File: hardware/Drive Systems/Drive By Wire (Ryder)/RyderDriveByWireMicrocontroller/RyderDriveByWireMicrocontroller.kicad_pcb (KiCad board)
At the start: 4 copper layers, 52.9 x 49.8 mm, 23 parts, among them J1 8P8C, J2 Conn_01x04_Male, J3 Conn_01x04_Male, J5 Conn_01x02_Male, J6 Conn_01x02_Male, J7 Conn_01x05_Pin, J8 Conn_ARM_SWD_TagConnect_TC203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, SW1 PTS526 SM15 SMTR2 LFS, U1 STM32G031F4Px, Y1 ECS-3225MVQ-160-BP-TR

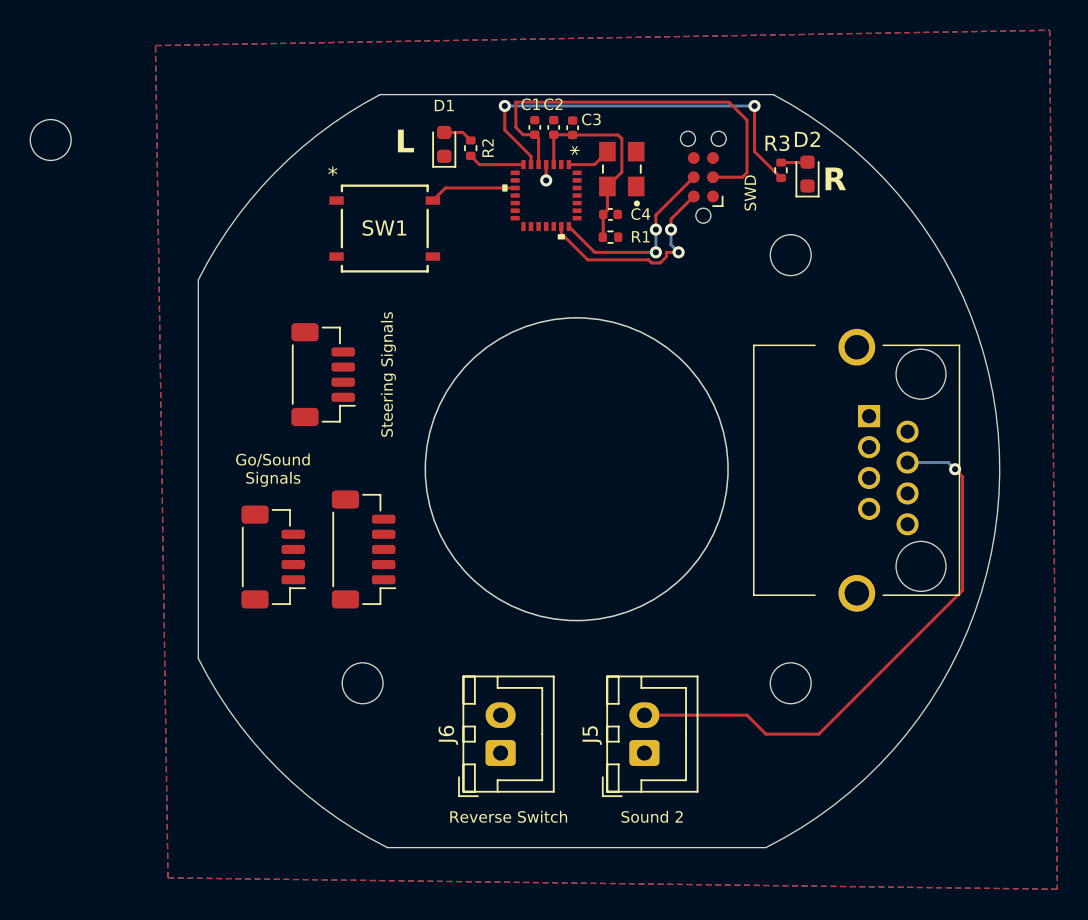
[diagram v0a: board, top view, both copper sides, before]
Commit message: moving drive by wire ryder pcb back into proper folder
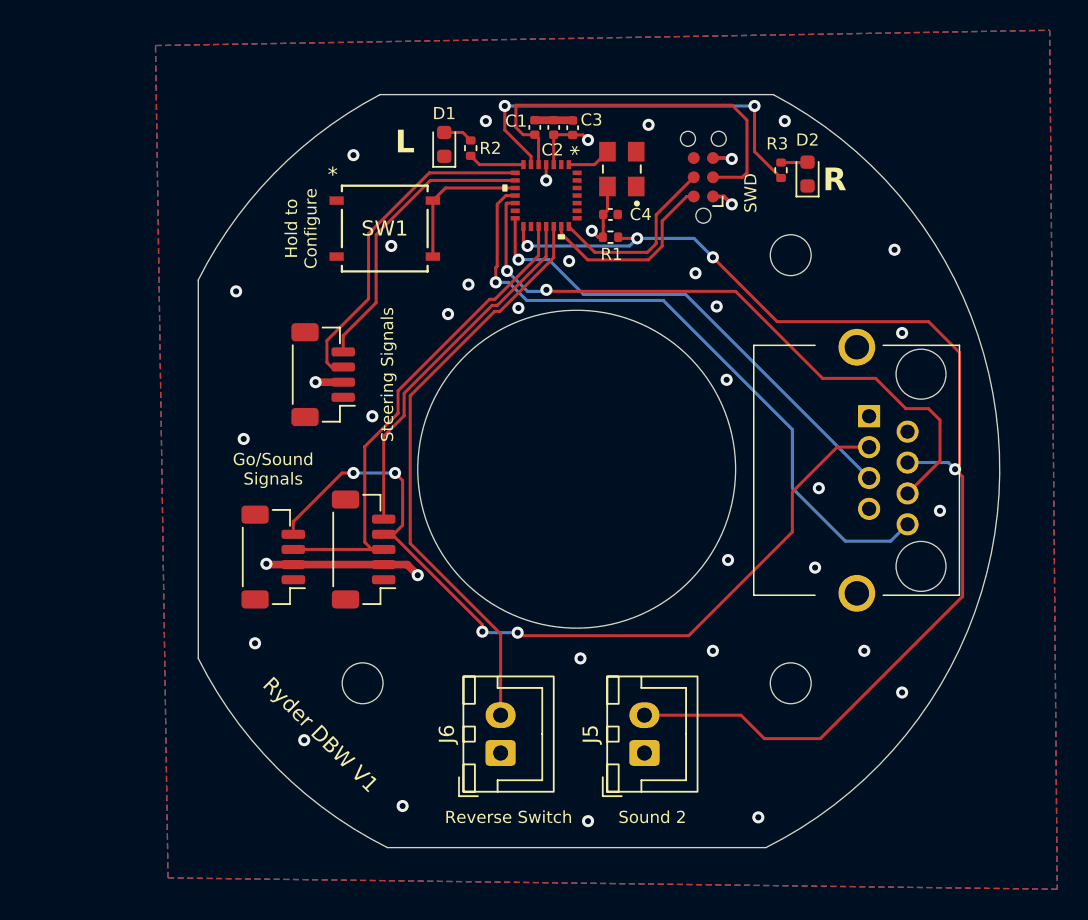
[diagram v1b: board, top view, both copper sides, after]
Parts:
- removed H2: MountingHole, MountingHole:MountingHole_2.7mm_M2.5
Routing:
- net Sound1: track 0.00 -> 55.9 mm, vias 0 -> 4
- net Other: track 0.00 -> 43.6 mm, vias 0 -> 1
- net JoyY: track 0.00 -> 43.6 mm, vias 0 -> 2
- net Sound2: track 37.0 -> 79.9 mm, vias 1 -> 4
- net ReverseSwitch: track 0.00 -> 38.9 mm
- net DriveButton: track 0.00 -> 33.2 mm
- net JoyX: track 0.00 -> 32.0 mm, vias 0 -> 1
- net AltReverseSwitch: track 0.00 -> 24.0 mm
- net SensorSin: track 0.00 -> 22.2 mm
- net SensorCos: track 0.00 -> 19.3 mm
- net +5V: track 0.00 -> 10.3 mm, vias 0 -> 2
- net GND: track 1.04 -> 4.82 mm, vias 1 -> 32
- net ConfigButton: track 5.78 -> 9.48 mm
- net +3V3: track 13.6 -> 12.0 mm, vias 0 -> 4
- net SWDIO: track 14.0 -> 12.6 mm, vias 2 -> 0
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- added copper zone on In2.Cu, net +3V3
- added copper zone on In2.Cu, net +5V
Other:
- outline, holes or cut-outs redrawn
- board text added: "Hold to Configure"
- board text added: "Ryder DBW V1"

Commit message: New Capacitive touch Control Panel PCB and a few tweaks to Ryder Steering wheel PCB
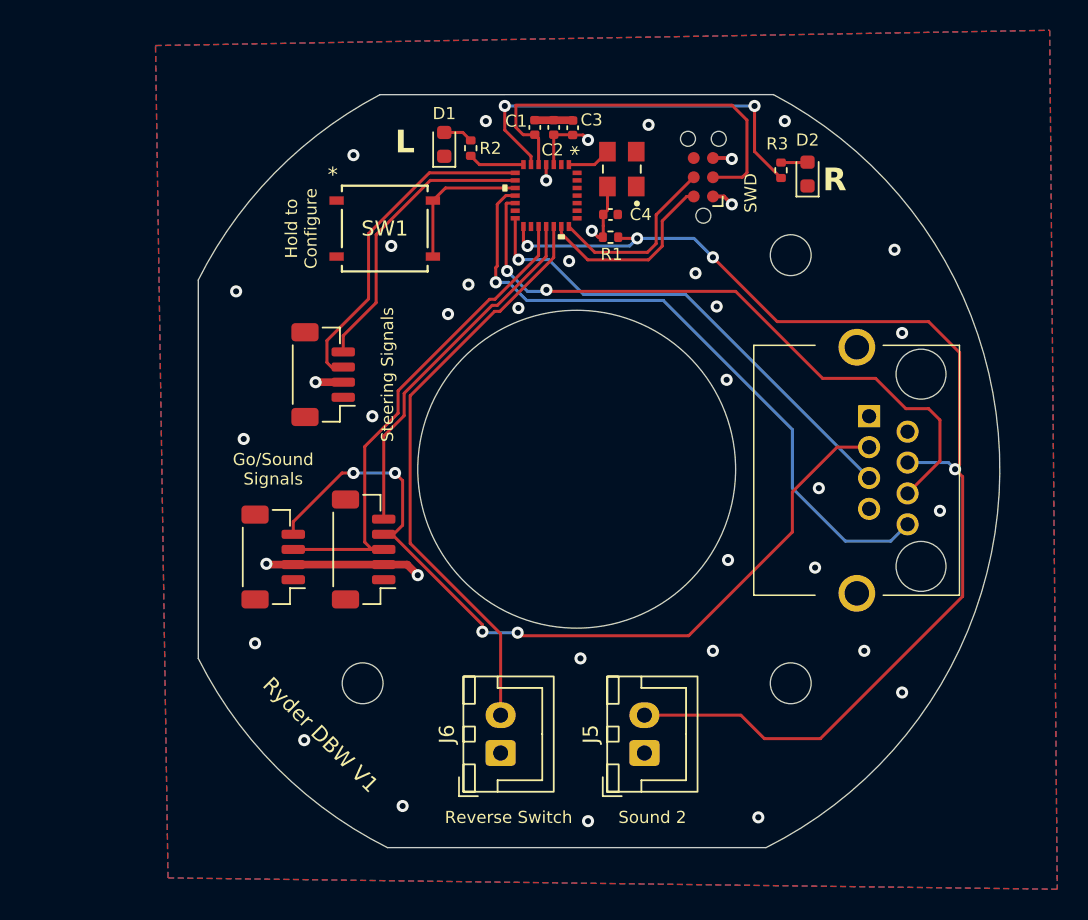
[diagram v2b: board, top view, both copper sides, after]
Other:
- board size 52.9 x 49.8 mm -> 53 x 49.8 mm
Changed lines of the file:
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@@
 	)
 	(gr_arc
-		(start 162.997401 75.254948)
-		(mid 177.949453 100.279467)
-		(end 162.5 125)
+		(start 163 75.25)
+		(mid 177.955042 100.279522)
+		(end 162.5025 125.004999)
 		(stroke
 			(width 0.05)
@@
 	(gr_line
 		(start 163 75.25)
-		(end 137 75.25)
+		(end 137.002599 75.25495)
 		(stroke
 			(width 0.05)
